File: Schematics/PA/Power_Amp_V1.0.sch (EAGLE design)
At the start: 101 parts, among them J1 4_PIN_AMPCONN, J12 1725724, J13 1725724, J14 1725724, J2 1984633, J3 2TERMINAL_SPEAKER, J4 2TERMINAL_SPEAKER, J5 2TERMINAL_SPEAKER, U1 LME49830, U2 LME49830, U3 LME49830

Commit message: added bstop and some silk screen
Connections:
- net LEFT renamed LEFT_IN
- net N$1 renamed BASS_IN
- net N$12 renamed BASS_OUT
- net N$75 renamed RIGHT_OUT
- net N$77 renamed LEFT_OUT
- net RIGHT renamed RIGHT_IN
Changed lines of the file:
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@@
 <?xml version="1.0" encoding="utf-8"?>
 <!DOCTYPE eagle SYSTEM "eagle.dtd">
-<eagle version="7.4.0">
+<eagle version="6.5.0">
 <drawing>
 <settings>
@@
 </segment>
 </net>
-<net name="N$75" class="0">
+<net name="RIGHT_OUT" class="0">
 <segment>
 <wire x1="447.04" y1="373.38" x2="447.04" y2="375.92" width="0.1524" layer="91"/>
@@
 </segment>
 </net>
-<net name="RIGHT" class="0">
+<net name="RIGHT_IN" class="0">
 <segment>
 <pinref part="R1" gate="G$1" pin="2"/>
@@
 </segment>
 </net>
-<net name="LEFT" class="0">
+<net name="LEFT_IN" class="0">
 <segment>
 <pinref part="J1" gate="G$1" pin="3"/>
@@
 </segment>
 </net>
-<net name="N$77" class="0">
+<net name="LEFT_OUT" class="0">
 <segment>
 <wire x1="497.84" y1="114.3" x2="497.84" y2="223.52" width="0.1524" layer="91"/>
@@
 </segment>
 </net>
-<net name="N$12" class="0">
+<net name="BASS_OUT" class="0">
 <segment>
 <wire x1="447.04" y1="233.68" x2="447.04" y2="236.22" width="0.1524" layer="91"/>
@@
 </segment>
 </net>
-<net name="N$1" class="0">
+<net name="BASS_IN" class="0">
 <segment>
 <pinref part="J1" gate="G$1" pin="2"/>

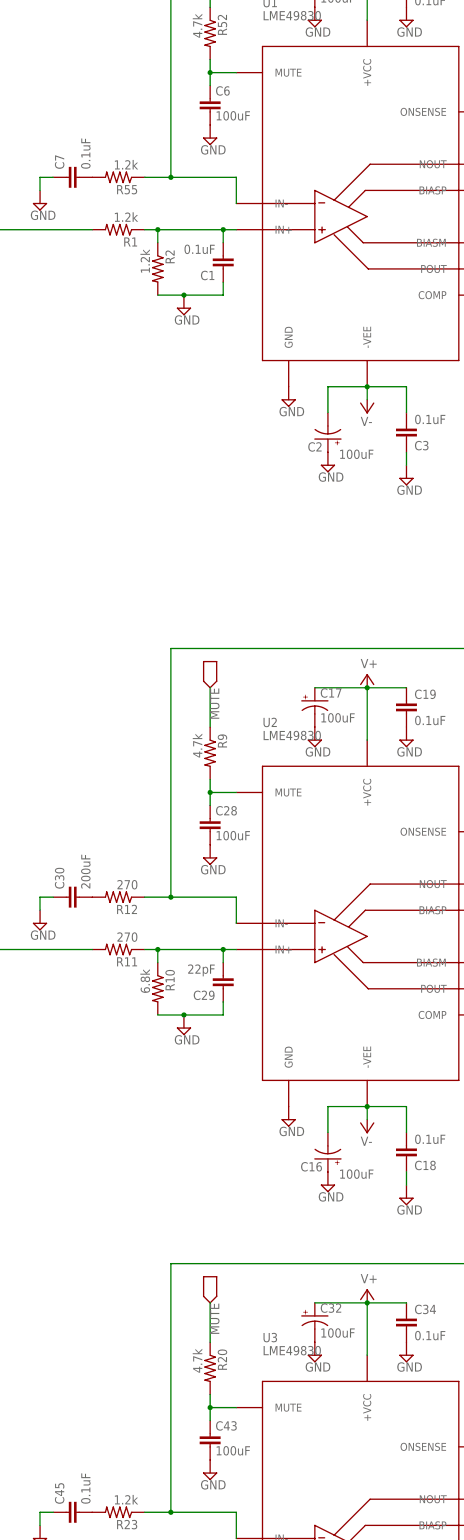
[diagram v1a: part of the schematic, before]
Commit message: changes footprint on mute cap
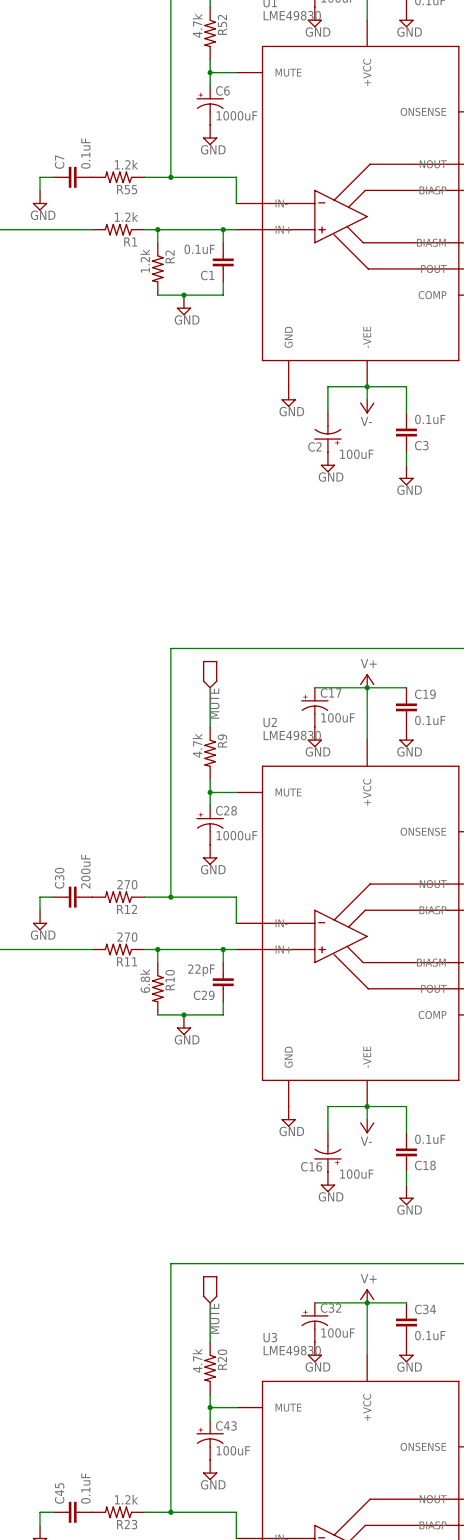
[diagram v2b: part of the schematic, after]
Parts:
- C28, C6: value 100uF -> 1000uF; device rcl:C-EU050-024X044 -> Amplifier_Parts:8MM_CAP_BSILK
- C43: device rcl:C-EU050-024X044 -> Amplifier_Parts:8MM_CAP_BSILK
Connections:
- net GND: now also C28.-, C43.-, C6.-; no longer C28.2, C43.2, C6.2
- net N$14: now also C28.+; no longer C28.1
- net N$37: now also C43.+; no longer C43.1
- net N$85: now also C6.+; no longer C6.1
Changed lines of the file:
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@@
 <part name="R51" library="rcl" deviceset="R-US_" device="0309/V" value="10"/>
 <part name="C15" library="rcl" deviceset="C-EU" device="050-024X044" value="0.1uF"/>
-<part name="C6" library="rcl" deviceset="C-EU" device="050-024X044" value="100uF"/>
+<part name="C6" library="Amplifier_Parts" deviceset="8MM_CAP_BSILK" device="" value="1000uF"/>
 <part name="R52" library="rcl" deviceset="R-US_" device="0204/2V" value="4.7k"/>
 <part name="GND22" library="supply2" deviceset="GND" device=""/>
@@
 <part name="R8" library="rcl" deviceset="R-US_" device="0309/V" value="10"/>
 <part name="C27" library="rcl" deviceset="C-EU" device="050-024X044" value="0.1uF"/>
-<part name="C28" library="rcl" deviceset="C-EU" device="050-024X044" value="100uF"/>
+<part name="C28" library="Amplifier_Parts" deviceset="8MM_CAP_BSILK" device="" value="1000uF"/>
 <part name="R9" library="rcl" deviceset="R-US_" device="0204/2V" value="4.7k"/>
 <part name="GND2" library="supply2" deviceset="GND" device=""/>
@@
 <part name="R19" library="rcl" deviceset="R-US_" device="0309/V" value="10"/>
 <part name="C42" library="rcl" deviceset="C-EU" device="050-024X044" value="0.1uF"/>
-<part name="C43" library="rcl" deviceset="C-EU" device="050-024X044" value="100uF"/>
+<part name="C43" library="Amplifier_Parts" deviceset="8MM_CAP_BSILK" device="" value="100uF"/>
 <part name="R20" library="rcl" deviceset="R-US_" device="0204/2V" value="4.7k"/>
 <part name="GND11" library="supply2" deviceset="GND" device=""/>
@@
 <pinref part="R52" gate="G$1" pin="2"/>
 <wire x1="330.2" y1="403.86" x2="330.2" y2="406.4" width="0.1524" layer="91"/>
-<pinref part="C6" gate="G$1" pin="1"/>
+<pinref part="C6" gate="G$1" pin="+"/>
 <wire x1="330.2" y1="403.86" x2="330.2" y2="401.32" width="0.1524" layer="91"/>
 <junction x="330.2" y="403.86"/>
@@
 <net name="GND" class="0">
 <segment>
-<pinref part="C6" gate="G$1" pin="2"/>
+<pinref part="C6" gate="G$1" pin="-"/>
 <pinref part="GND22" gate="GND" pin="GND"/>
 </segment>
@@
 </segment>
 <segment>
-<pinref part="C28" gate="G$1" pin="2"/>
+<pinref part="C28" gate="G$1" pin="-"/>
 <pinref part="GND2" gate="GND" pin="GND"/>
 </segment>
@@
 </segment>
 <segment>
-<pinref part="C43" gate="G$1" pin="2"/>
+<pinref part="C43" gate="G$1" pin="-"/>
 <pinref part="GND11" gate="GND" pin="GND"/>
 </segment>
@@
 <pinref part="R9" gate="G$1" pin="2"/>
 <wire x1="330.2" y1="264.16" x2="330.2" y2="266.7" width="0.1524" layer="91"/>
-<pinref part="C28" gate="G$1" pin="1"/>
+<pinref part="C28" gate="G$1" pin="+"/>
 <wire x1="330.2" y1="264.16" x2="330.2" y2="261.62" width="0.1524" layer="91"/>
 <junction x="330.2" y="264.16"/>
@@
 <pinref part="R20" gate="G$1" pin="2"/>
 <wire x1="330.2" y1="144.78" x2="330.2" y2="147.32" width="0.1524" layer="91"/>
-<pinref part="C43" gate="G$1" pin="1"/>
+<pinref part="C43" gate="G$1" pin="+"/>
 <wire x1="330.2" y1="144.78" x2="330.2" y2="142.24" width="0.1524" layer="91"/>
 <junction x="330.2" y="144.78"/>

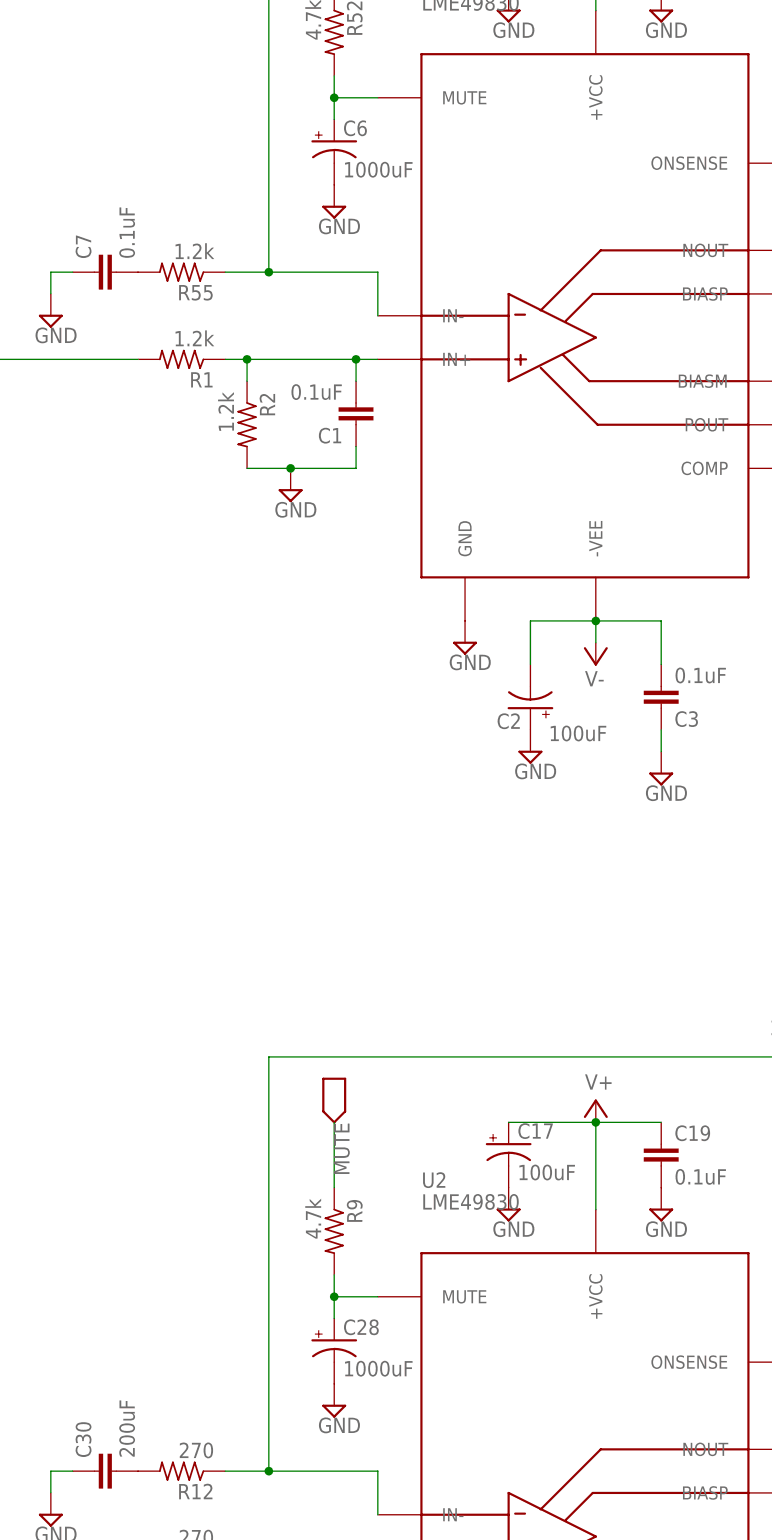
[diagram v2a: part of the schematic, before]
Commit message: updated PA
updated footprint for mute cap
added logo
changed silkscreen
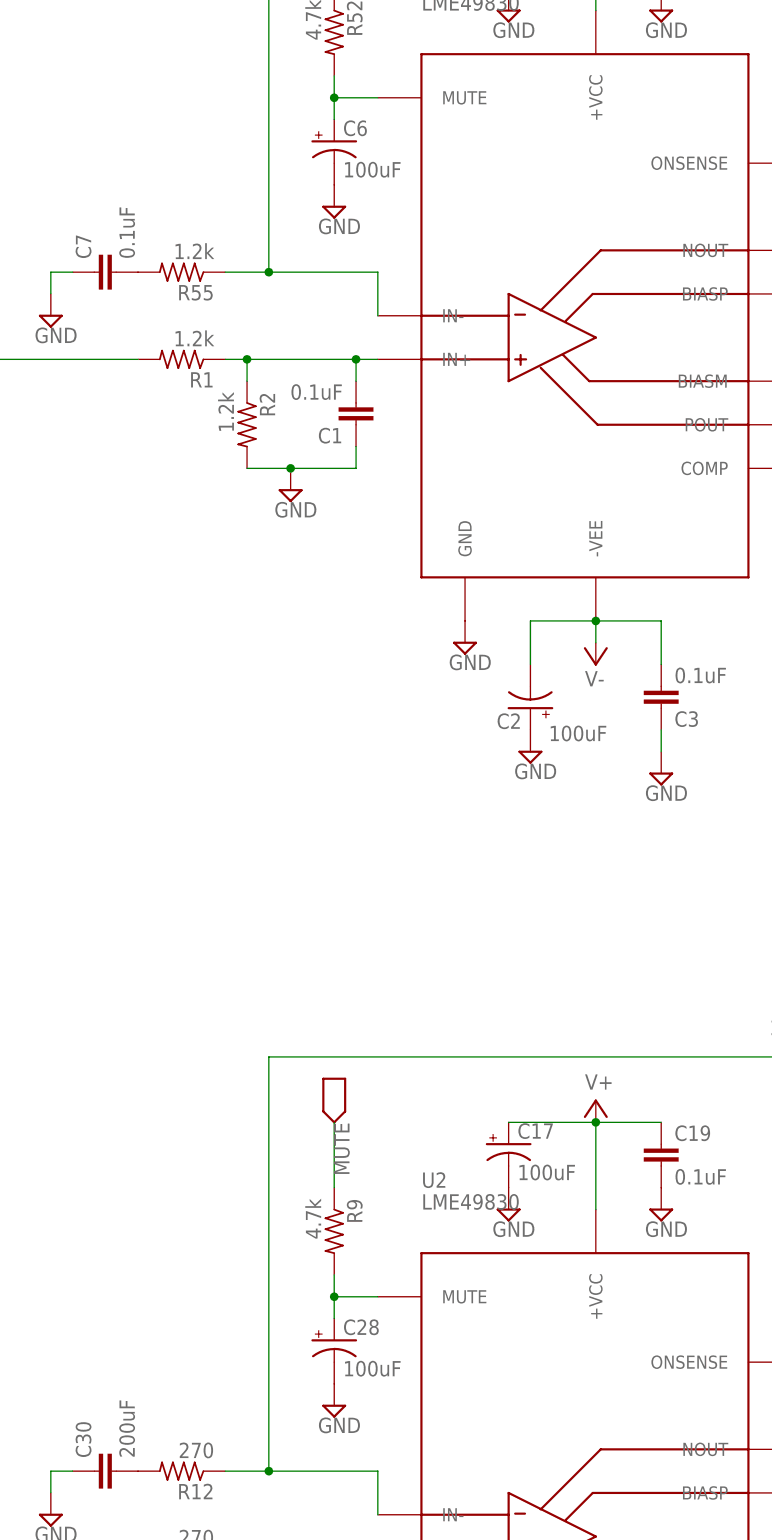
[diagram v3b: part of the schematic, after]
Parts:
- C28, C6: value 1000uF -> 100uF; device Amplifier_Parts:8MM_CAP_BSILK -> rcl:CPOL-USE2.5-6
- C43: device Amplifier_Parts:8MM_CAP_BSILK -> rcl:CPOL-USE2.5-6
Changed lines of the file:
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@@
 <?xml version="1.0" encoding="utf-8"?>
 <!DOCTYPE eagle SYSTEM "eagle.dtd">
-<eagle version="6.5.0">
+<eagle version="7.4.0">
 <drawing>
 <settings>
@@
 <part name="R51" library="rcl" deviceset="R-US_" device="0309/V" value="10"/>
 <part name="C15" library="rcl" deviceset="C-EU" device="050-024X044" value="0.1uF"/>
-<part name="C6" library="Amplifier_Parts" deviceset="8MM_CAP_BSILK" device="" value="1000uF"/>
+<part name="C6" library="rcl" deviceset="CPOL-US" device="E2.5-6" value="100uF"/>
 <part name="R52" library="rcl" deviceset="R-US_" device="0204/2V" value="4.7k"/>
 <part name="GND22" library="supply2" deviceset="GND" device=""/>
@@
 <part name="R8" library="rcl" deviceset="R-US_" device="0309/V" value="10"/>
 <part name="C27" library="rcl" deviceset="C-EU" device="050-024X044" value="0.1uF"/>
-<part name="C28" library="Amplifier_Parts" deviceset="8MM_CAP_BSILK" device="" value="1000uF"/>
+<part name="C28" library="rcl" deviceset="CPOL-US" device="E2.5-6" value="100uF"/>
 <part name="R9" library="rcl" deviceset="R-US_" device="0204/2V" value="4.7k"/>
 <part name="GND2" library="supply2" deviceset="GND" device=""/>
@@
 <part name="R19" library="rcl" deviceset="R-US_" device="0309/V" value="10"/>
 <part name="C42" library="rcl" deviceset="C-EU" device="050-024X044" value="0.1uF"/>
-<part name="C43" library="Amplifier_Parts" deviceset="8MM_CAP_BSILK" device="" value="100uF"/>
+<part name="C43" library="rcl" deviceset="CPOL-US" device="E2.5-6" value="100uF"/>
 <part name="R20" library="rcl" deviceset="R-US_" device="0204/2V" value="4.7k"/>
 <part name="GND11" library="supply2" deviceset="GND" device=""/>
